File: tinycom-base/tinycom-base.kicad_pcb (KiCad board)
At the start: 2 copper layers, 45.2 x 45.2 mm, 38 parts, among them J1 MICRO_SD_HINGE, P1 CONN_02X08, P2 CONN_02X08, P3 USB_A, P4 USB_B, U1 SY8008BAAC, U2 SY8008BAAC, U3 SY8008BAAC

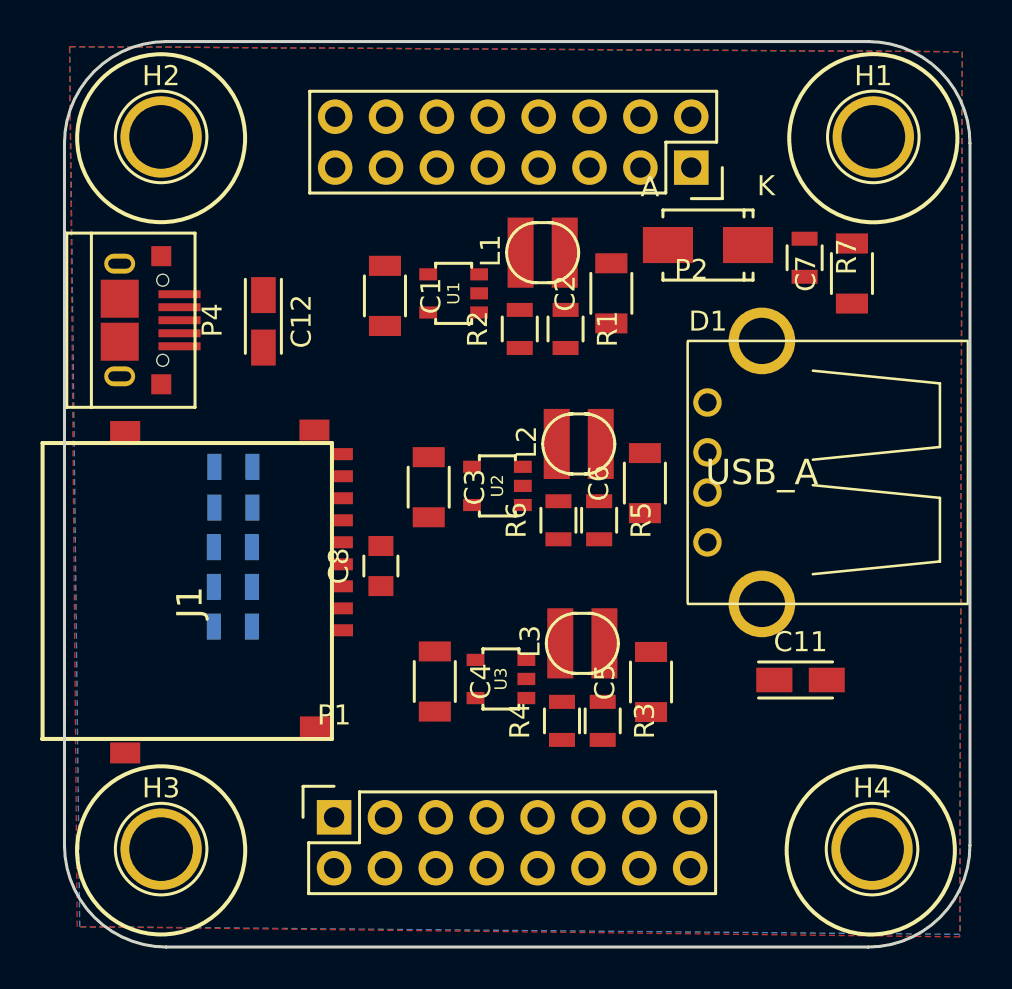
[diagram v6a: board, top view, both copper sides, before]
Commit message: route base usb+sdcard
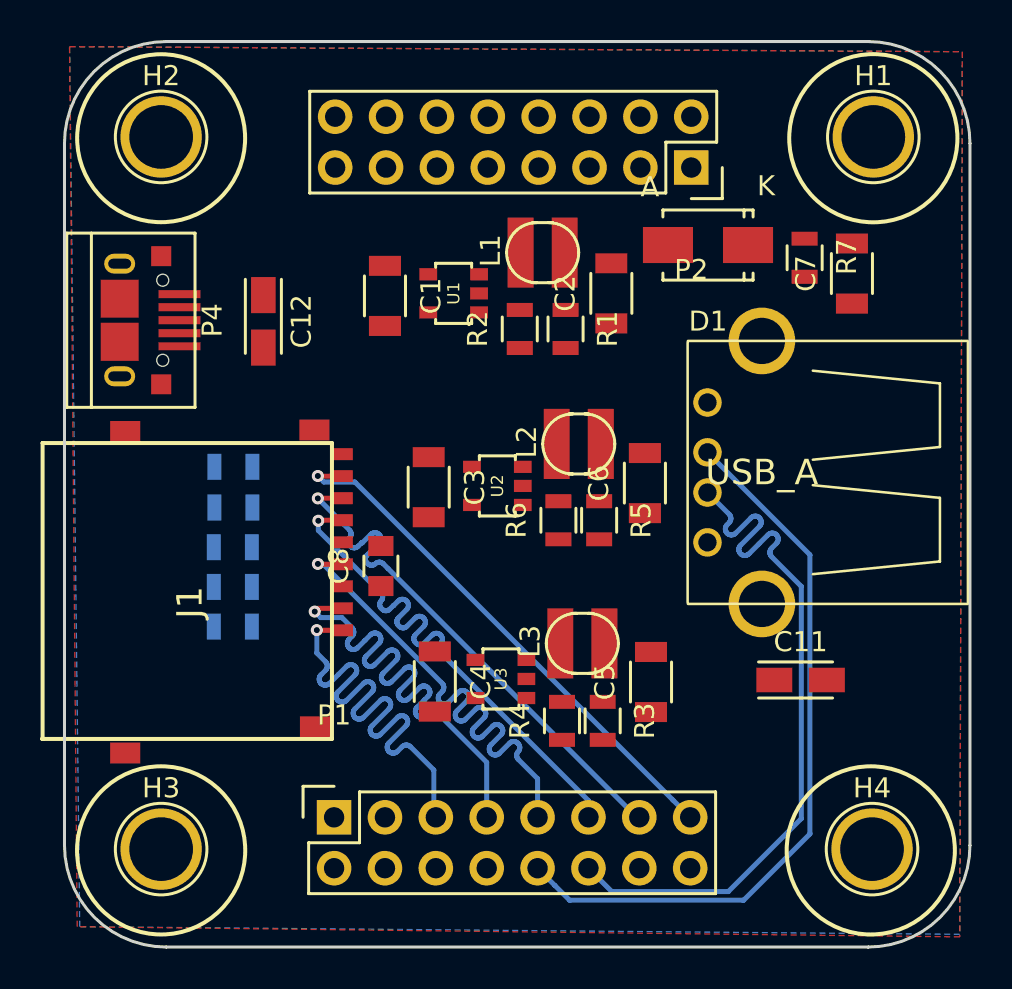
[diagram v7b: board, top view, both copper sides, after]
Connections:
- P3 pad 5: Net-(P3-Pad5) -> GND
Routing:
- net UDP1: track 0.00 -> 36.8 mm
- net UDM1: track 0.00 -> 36.8 mm
- net SDC0_D2: track 0.00 -> 26.9 mm, vias 0 -> 1
- net SDC0_D3: track 0.00 -> 26.9 mm, vias 0 -> 1
- net SDC0_CMD: track 0.00 -> 26.8 mm, vias 0 -> 1
- net SDC0_D0: track 0.00 -> 26.8 mm, vias 0 -> 1
- net SDC0_D1: track 0.00 -> 26.8 mm, vias 0 -> 1
- net SDC0_CLK: track 0.00 -> 26.7 mm, vias 0 -> 1
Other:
- net class Default: clearance 0.2 -> 0.18
- rule trace_clearance: 0.2 -> 0.18

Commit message: done update base board
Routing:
- net VCC_33: track 0.00 -> 95.8 mm, vias 0 -> 1
- net +5V: track 0.00 -> 66.6 mm
- net VCC_14: track 0.00 -> 44.9 mm
- net UDM0: track 0.00 -> 43.2 mm, vias 0 -> 1
- net UDP0: track 0.00 -> 43.1 mm, vias 0 -> 1
- net VCC_15: track 0.00 -> 23.6 mm
- net GND: track 0.00 -> 20.8 mm, vias 0 -> 2
- net VCC_30: track 0.00 -> 15.2 mm
- net Net-(R1-Pad2): track 0.00 -> 7.95 mm
- net Net-(R3-Pad2): track 0.00 -> 7.57 mm
- net Net-(R5-Pad2): track 0.00 -> 7.42 mm
- net SDC0_CMD: track 26.8 -> 30.6 mm
- net SDC0_D1: track 26.8 -> 30.5 mm
- net SDC0_D0: track 26.8 -> 30.5 mm
- net SDC0_D3: track 26.9 -> 30.3 mm
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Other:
- net class Default: clearance 0.18 -> 0.15
- rule trace_clearance: 0.18 -> 0.15
